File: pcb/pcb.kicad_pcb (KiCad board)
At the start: 2 copper layers, 2 parts, among them U1 ATtiny85-20P

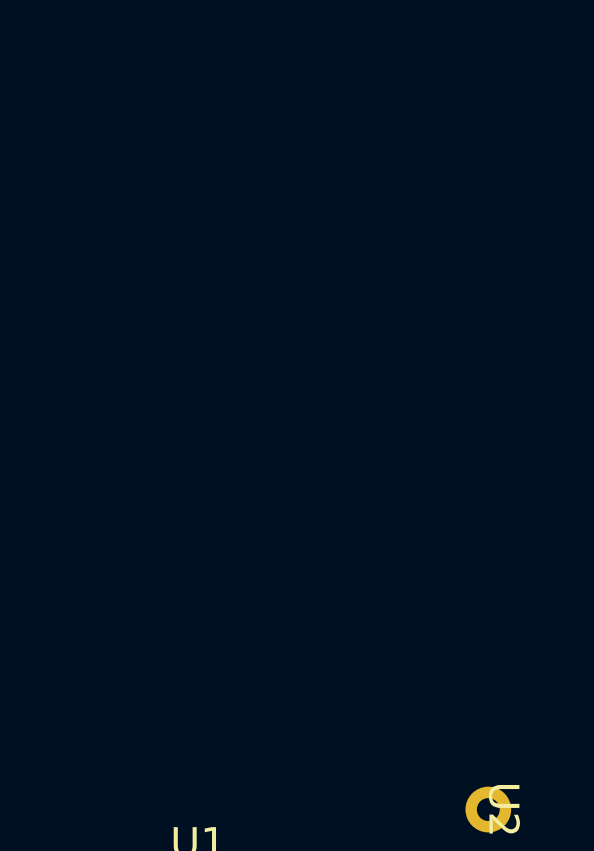
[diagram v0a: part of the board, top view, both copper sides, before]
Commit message: Add schematic
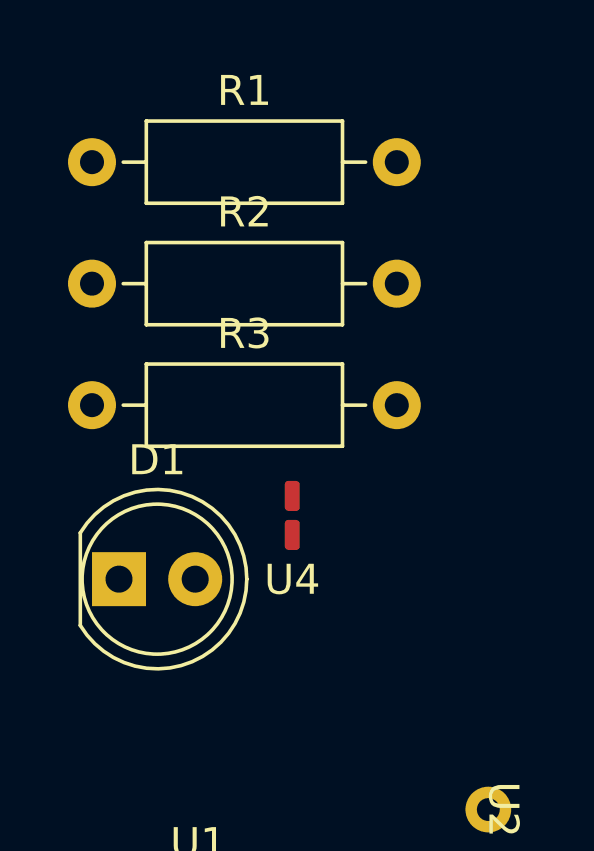
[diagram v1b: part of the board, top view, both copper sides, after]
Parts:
- added D1: LED, LED_THT:LED_D5.0mm, F.Cu at (131.6, 79.1)
- added R1: 10k, Resistor_THT:R_Axial_DIN0207_L6.3mm_D2.5mm_P10.16mm_Horizontal, F.Cu at (130.7, 65.2)
- added R2: 1M, Resistor_THT:R_Axial_DIN0207_L6.3mm_D2.5mm_P10.16mm_Horizontal, F.Cu at (130.7, 69.2)
- added R3: 220, Resistor_THT:R_Axial_DIN0207_L6.3mm_D2.5mm_P10.16mm_Horizontal, F.Cu at (130.7, 73.3)
- added U4: ~, Library:Jumper, F.Cu at (137.4, 77.6)
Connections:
- U1 pad 2: unconnected-(U1-XTAL1/PB3-Pad2) -> Net-(U1-XTAL1/PB3)
- U1 pad 3: unconnected-(U1-XTAL2/PB4-Pad3) -> Net-(BZ1-+)

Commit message: Add PCB draft
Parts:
- removed U4: ~, Library:Jumper
- added BZ1: Buzzer, Buzzer_Beeper:Buzzer_15x7.5RM7.6, F.Cu at (135.6, 82.8)
- added SW1: SW_Push, Button_Switch_THT:SW_PUSH_6mm, F.Cu at (123.6, 112.2)
- added U3: ~, Library:Piezo, F.Cu at (134.0, 104.8)
- moved R2 34.5 mm to (120.0, 102.0), turned to 90 degrees
- moved D1 30.1 mm to (120.0, 106.9)
- moved R1 28.7 mm to (140.2, 92.3), turned to -90 degrees
- moved R3 19.7 mm to (124.2, 91.9), turned to -90 degrees
- moved U2 6.12 mm to (147.1, 92.0)
- moved U1 4.10 mm to (127.7, 93.2)
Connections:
- R3 pad 1: Net-(R3-Pad1) -> Net-(U1-PB1)

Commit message: Finish PCB design
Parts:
- moved U3 48.8 mm to (100.5, 140.2), turned to 90 degrees
- moved R1 44.7 mm to (103.6, 118.0)
- moved U2 40.8 mm to (107.7, 102.5), turned to 0 degrees
- moved R3 36.1 mm to (99.2, 118.0)
- moved U1 29.7 mm to (105.5, 113.0), turned to 90 degrees
- moved BZ1 28.8 mm to (124.2, 109.2), turned to -90 degrees
- moved R2 19.9 mm to (108.0, 118.0), turned to -90 degrees
- moved D1 18.5 mm to (129.5, 122.8), turned to -90 degrees
- moved SW1 15.0 mm to (112.0, 121.8), turned to 0 degrees
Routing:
- net Net-(U1-PB2): track 0.00 -> 54.0 mm
- net GND: track 0.00 -> 36.0 mm
- net Net-(U1-~{RESET}/PB5): track 0.00 -> 32.9 mm
- net Net-(D1-A): track 0.00 -> 32.7 mm
- net +5V: track 0.00 -> 29.9 mm
- net Net-(U1-PB1): track 0.00 -> 25.7 mm
- net Net-(BZ1-+): track 0.00 -> 20.3 mm
- net Net-(U3-+): track 0.00 -> 16.3 mm
- net (no net): track 0.00 -> 15.2 mm
- net Net-(U1-XTAL1/PB3): track 0.00 -> 6.84 mm
- net Net-(U1-AREF/PB0): track 0.00 -> 5.95 mm
- added copper zone on B.Cu, net GND
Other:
- board outline added: 36 x 53.5 mm
